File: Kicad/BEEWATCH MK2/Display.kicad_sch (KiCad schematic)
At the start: 6 parts, among them J3 Conn_02x06_Odd_Even, Q2 DMG6968U

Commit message: Deep optmization 90% completed
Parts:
- J3: footprint Connector_PinHeader_1.27mm:PinHeader_2x06_P1.27mm_Vertical -> Connector_PinHeader_1.27mm:PinHeader_2x06_P1.27mm_Vertical_SMD
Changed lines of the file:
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@@
 			)
 		)
-		(property "Footprint" "Connector_PinHeader_1.27mm:PinHeader_2x06_P1.27mm_Vertical"
+		(property "Footprint" "Connector_PinHeader_1.27mm:PinHeader_2x06_P1.27mm_Vertical_SMD"
 			(at 160.02 96.52 0)
 			(effects

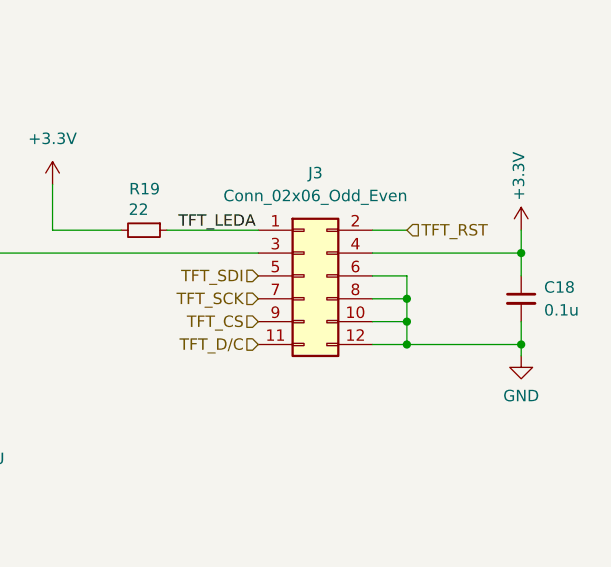
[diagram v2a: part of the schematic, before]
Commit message: Added display board schema
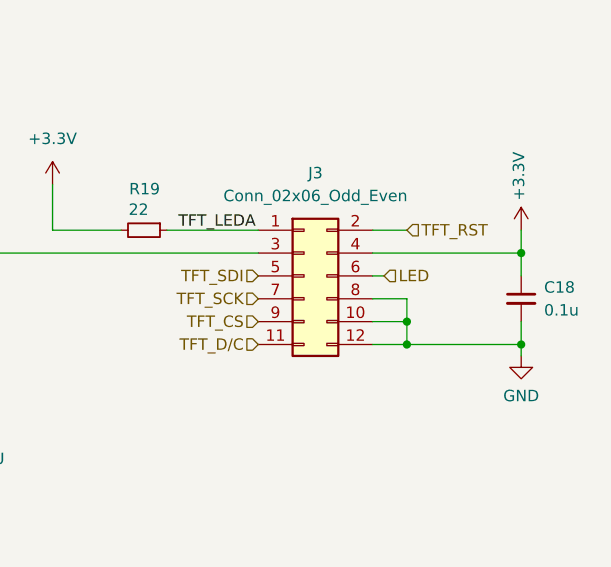
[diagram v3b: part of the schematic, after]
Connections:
- net GND: no longer J3.6 (Pin_6)
- new net LED: J3.6 (Pin_6)
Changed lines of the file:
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@@
-	)
-	(junction
-		(at 171.45 99.06)
-		(diameter 0)
-		(color 0 0 0 0)
 	)
 	(junction
@@
 	(wire
 		(pts
+			(xy 167.64 96.52) (xy 168.91 96.52)
+		)
+		(stroke
+			(width 0)
+			(type default)
+		)
+	)
+	(wire
+		(pts
 			(xy 100.33 97.79) (xy 100.33 106.68)
 		)
@@
 	(wire
 		(pts
-			(xy 171.45 96.52) (xy 171.45 99.06)
-		)
-		(stroke
-			(width 0)
-			(type default)
-		)
-	)
-	(wire
-		(pts
 			(xy 132.08 86.36) (xy 132.08 91.44)
 		)
@@
 		(pts
 			(xy 167.64 101.6) (xy 171.45 101.6)
-		)
-		(stroke
-			(width 0)
-			(type default)
-		)
-	)
-	(wire
-		(pts
-			(xy 167.64 96.52) (xy 171.45 96.52)
 		)
 		(stroke
@@
 		)
 	)
+	(hierarchical_label "LED"
+		(shape input)
+		(at 168.91 96.52 0)
+		(effects
+			(font
+				(size 1.27 1.27)
+			)
+			(justify left)
+		)
+	)

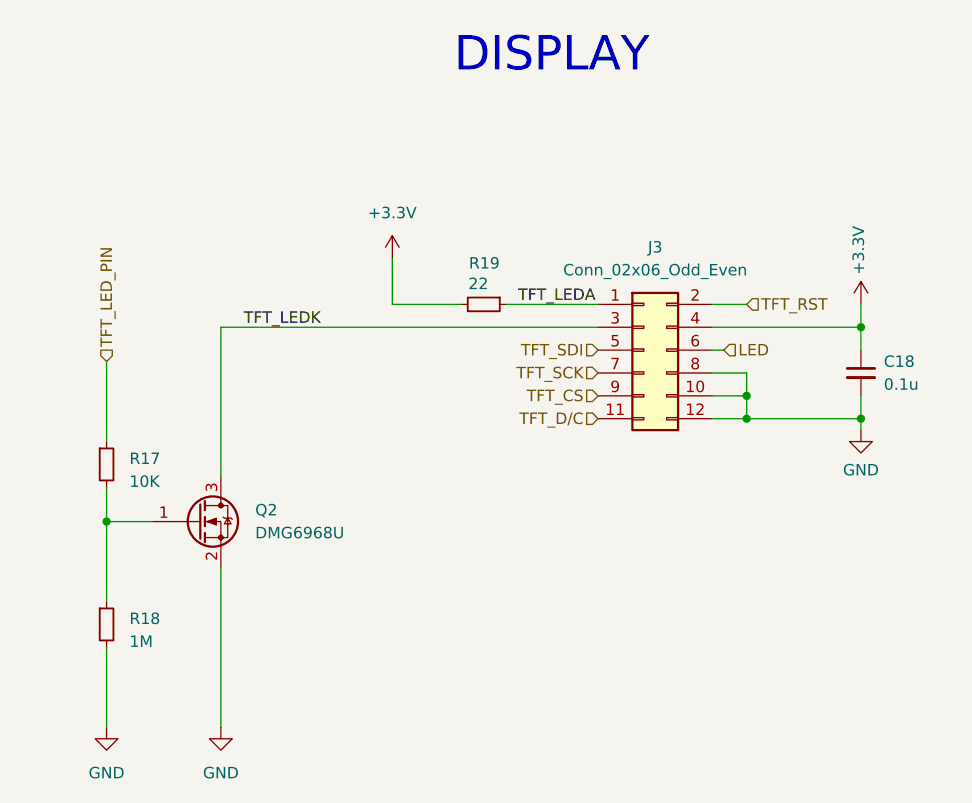
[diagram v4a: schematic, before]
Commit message: Updating MPN
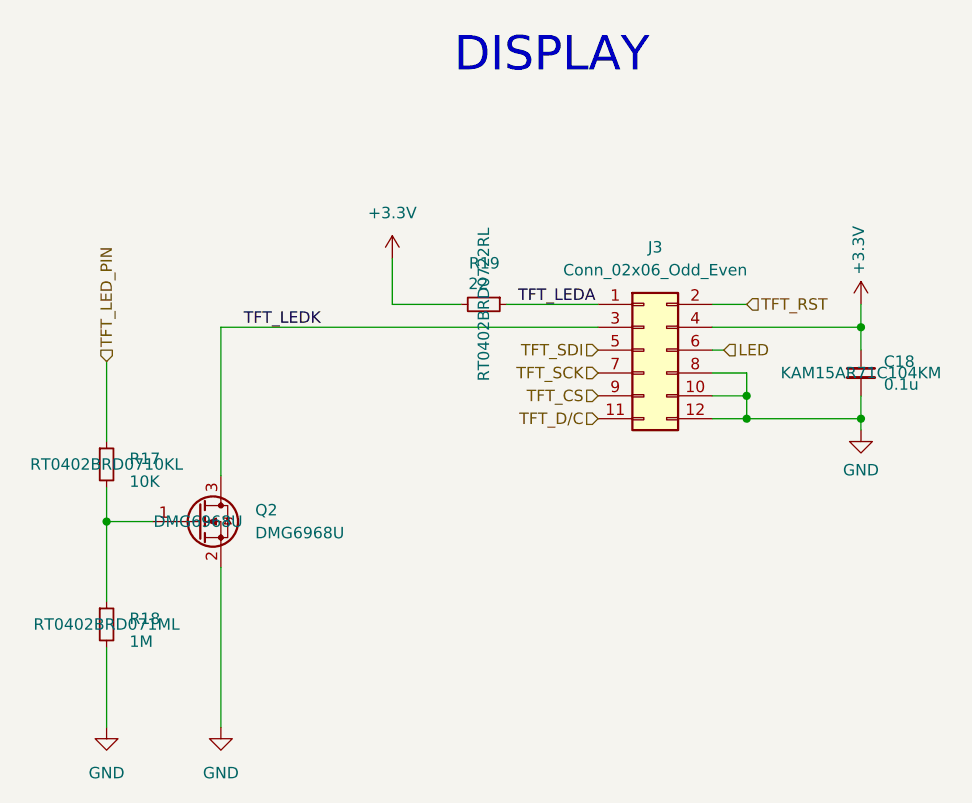
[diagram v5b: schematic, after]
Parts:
- C18: MPN (none) -> KAM15AR71C104KM
- Q2: MPN (none) -> DMG6968U
- R17: MPN (none) -> RT0402BRD0710KL
- R18: MPN (none) -> RT0402BRD071ML
- R19: MPN (none) -> RT0402BRD0722RL
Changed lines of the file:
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@@
 			)
 		)
-		(property "MPN" ""
+		(property "MPN" "KAM15AR71C104KM"
 			(at 184.15 99.06 0)
 			(effects
@@
 			)
 		)
-		(property "MPN" ""
+		(property "MPN" "RT0402BRD0710KL "
 			(at 100.33 109.22 0)
 			(effects
@@
 			)
 		)
-		(property "MPN" ""
+		(property "MPN" "DMG6968U"
 			(at 110.49 115.57 0)
 			(effects
@@
 			)
 		)
-		(property "MPN" ""
+		(property "MPN" "RT0402BRD071ML "
 			(at 100.33 127 0)
 			(effects
@@
 			)
 		)
-		(property "MPN" ""
+		(property "MPN" "RT0402BRD0722RL "
 			(at 142.24 91.44 0)
 			(effects
